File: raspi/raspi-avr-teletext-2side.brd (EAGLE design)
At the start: 36.8 x 23.2 mm, 17 parts, among them U1 ATMEGA328P, U2 EL1883, X1 WBTOR1

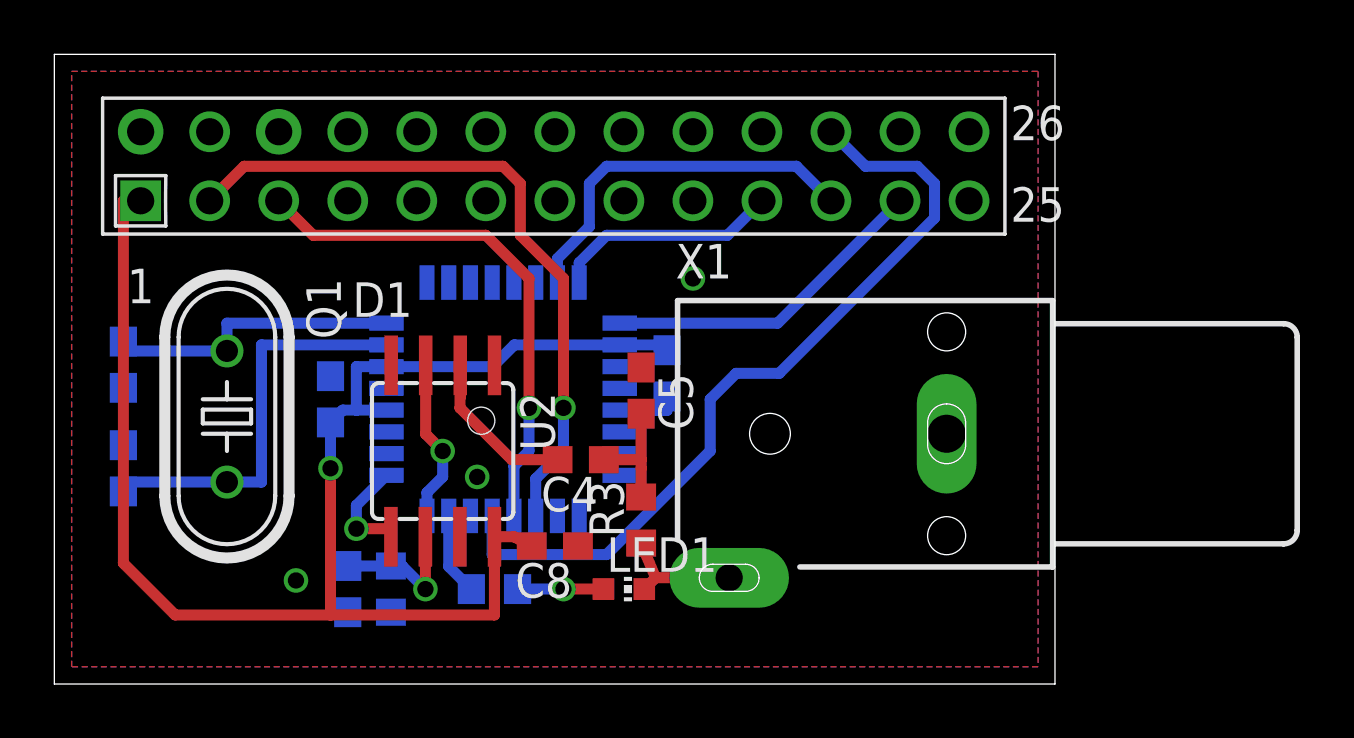
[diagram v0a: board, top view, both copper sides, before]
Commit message: Fix MOSI/MISO
I can never remember whether you are supposed to flip these or not.
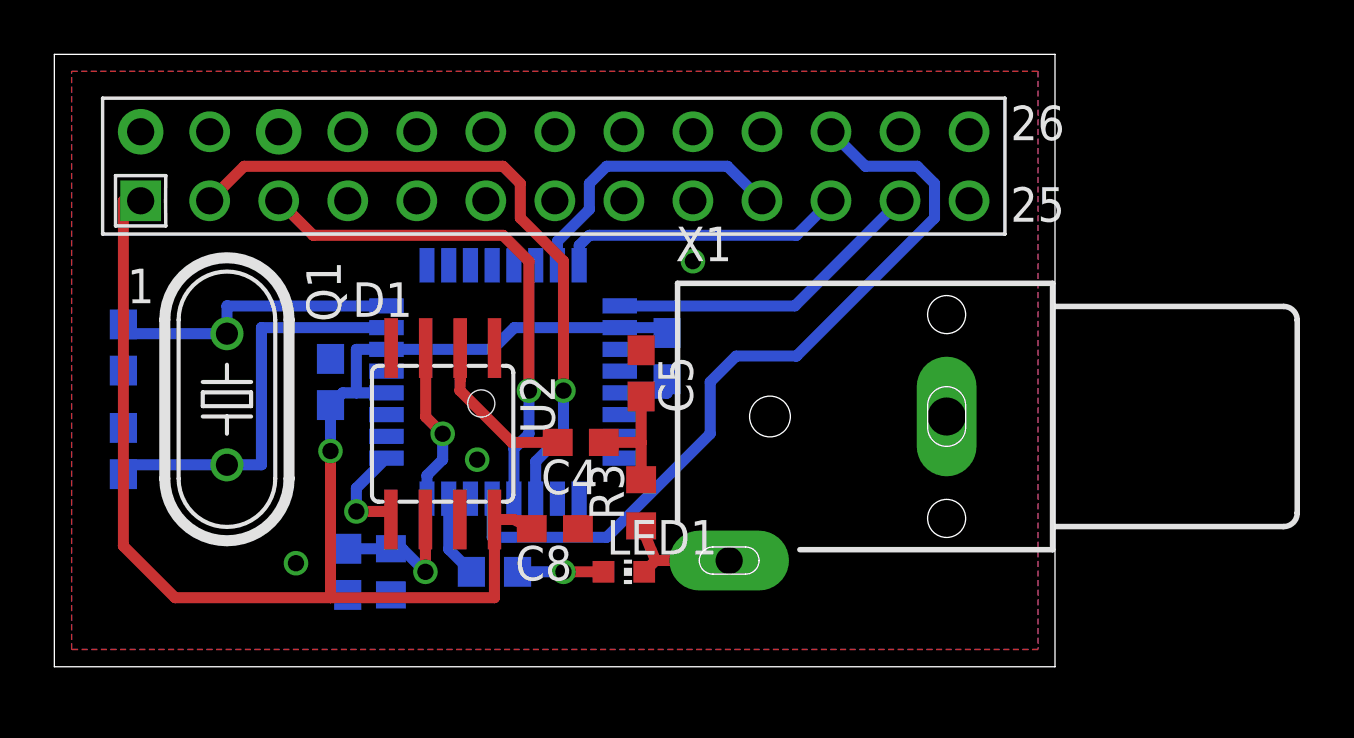
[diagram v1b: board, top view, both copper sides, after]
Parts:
- moved C1 0.64 mm to (8.26, 56.8)
- moved C3 0.64 mm to (16.5, 52.4)
- moved C6 0.64 mm to (15.9, 59.4)
- moved C7 0.64 mm to (28.3, 60.3)
- moved LED1 0.64 mm to (26.7, 52.4)
- moved R1 0.64 mm to (21.9, 52.4)
- moved R2 0.64 mm to (18.1, 52.4)
- moved R3 0.64 mm to (27.3, 54.9)
- moved U1 0.64 mm to (22.2, 59.4)
- moved C2 0.63 mm to (8.26, 60.6)
- moved C4 0.63 mm to (25.1, 57.1)
- moved C5 0.63 mm to (27.3, 59.7)
- moved C8 0.63 mm to (24.1, 54.0)
- moved Q1 0.63 mm to (12.1, 58.7)
- moved U2 0.63 mm to (20.0, 57.5)
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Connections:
- net MISO: now also D1.21; no longer D1.19
- net MOSI: now also D1.19; no longer D1.21
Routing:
- net MOSI: track 13.8 -> 10.6 mm
- net MISO: track 8.40 -> 10.7 mm
- net VCC: track 55.8 -> 55.2 mm
- net SDA: track 25.5 -> 24.9 mm
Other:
- board size 36.8 x 23.2 mm -> 36.8 x 22.5 mm
